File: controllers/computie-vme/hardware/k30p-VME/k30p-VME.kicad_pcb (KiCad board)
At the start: 2 copper layers, 160 x 100 mm, 87 parts, among them J1 5V, J2 5V, J3 JTAG, J4 Serial1, J5 Serial2, P1 USB_C_Plug_USB2.0, P2 USB_C_Plug_USB2.0, P3 VME64-P1-3R, SW1 ~{RESET}, SW2 SW_DIP_x06, SW3 E-Switch TL2243, U1 MC68030RC, U10 FT231XS, U11 74ABT16245DL, U12 74ABT16245DL, U13 74ABT16245DL, U14 74ABT16245DL, U15 74ABT16245DL, U16 74HC148, U2 74HC14, U3 74HC05, U4 ATF1508AS-xxAx100, U5 AS6C8016, U6 AS6C8016, U7 AM29F040, U8 MC68681, U9 FT231XS, Y1 Crystal, Y2 Crystal

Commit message: Updating with more work in progress
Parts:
- removed the D2 at (115.2, 124.0)
- removed the SW2 at (96.3, 46.1)
- added C12: 0.1uF, Capacitor_SMD:C_0805_2012Metric_Pad1.18x1.45mm_HandSolder, F.Cu at (69.8, 48.1)
- added C13: 0.1uF, Capacitor_SMD:C_0805_2012Metric_Pad1.18x1.45mm_HandSolder, F.Cu at (103.6, 36.6)
- added C14: 0.1uF, Capacitor_SMD:C_0805_2012Metric_Pad1.18x1.45mm_HandSolder, F.Cu at (88.0, 64.9)
- added C15: 0.1uF, Capacitor_SMD:C_0805_2012Metric_Pad1.18x1.45mm_HandSolder, F.Cu at (86.9, 88.8)
- added C16: 0.1uF, Capacitor_SMD:C_0805_2012Metric_Pad1.18x1.45mm_HandSolder, F.Cu at (122.2, 46.6)
- added C17: 0.1uF, Capacitor_SMD:C_0805_2012Metric_Pad1.18x1.45mm_HandSolder, F.Cu at (128.8, 46.4)
- added C18: 0.1uF, Capacitor_SMD:C_0805_2012Metric_Pad1.18x1.45mm_HandSolder, F.Cu at (159.2, 63.8)
- added C19: 0.1uF, Capacitor_SMD:C_0805_2012Metric_Pad1.18x1.45mm_HandSolder, F.Cu at (128.0, 89.4)
- added C20: 0.1uF, Capacitor_SMD:C_0805_2012Metric_Pad1.18x1.45mm_HandSolder, F.Cu at (145.5, 89.3)
- added C21: 0.1uF, Capacitor_SMD:C_0805_2012Metric_Pad1.18x1.45mm_HandSolder, F.Cu at (151.1, 101.0)
- added C22: 0.1uF, Capacitor_SMD:C_0805_2012Metric_Pad1.18x1.45mm_HandSolder, F.Cu at (123.7, 106.9)
- added C23: 0.1uF, Capacitor_SMD:C_0805_2012Metric_Pad1.18x1.45mm_HandSolder, F.Cu at (159.1, 114.7)
- added C24: 0.1uF, Capacitor_SMD:C_0805_2012Metric_Pad1.18x1.45mm_HandSolder, F.Cu at (114.2, 114.8)
- added C25: 0.1uF, Capacitor_SMD:C_0805_2012Metric_Pad1.18x1.45mm_HandSolder, F.Cu at (162.9, 37.5)
- added C26: 0.1uF, Capacitor_SMD:C_0805_2012Metric_Pad1.18x1.45mm_HandSolder, F.Cu at (162.9, 53.2)
- added C27: 0.1uF, Capacitor_SMD:C_0805_2012Metric_Pad1.18x1.45mm_HandSolder, F.Cu at (162.9, 69.3)
- added C28: 0.1uF, Capacitor_SMD:C_0805_2012Metric_Pad1.18x1.45mm_HandSolder, F.Cu at (162.9, 85.2)
- added C29: 0.1uF, Capacitor_SMD:C_0805_2012Metric_Pad1.18x1.45mm_HandSolder, F.Cu at (162.9, 101.1)
- added C30: 0.1uF, Capacitor_SMD:C_0805_2012Metric_Pad1.18x1.45mm_HandSolder, B.Cu at (141.9, 63.5)
- added C31: 0.1uF, Capacitor_SMD:C_0805_2012Metric_Pad1.18x1.45mm_HandSolder, B.Cu at (134.2, 63.5)
- added C32: 0.1uF, Capacitor_SMD:C_0805_2012Metric_Pad1.18x1.45mm_HandSolder, B.Cu at (141.9, 71.2)
- added C33: 0.1uF, Capacitor_SMD:C_0805_2012Metric_Pad1.18x1.45mm_HandSolder, B.Cu at (134.2, 71.2)
- added JP5: BG0IN, Connector_PinHeader_2.54mm:PinHeader_1x02_P2.54mm_Vertical, F.Cu at (110.9, 94.5)
- added JP6: BG0OUT, Connector_PinHeader_2.54mm:PinHeader_1x02_P2.54mm_Vertical, F.Cu at (114.6, 94.5)
- added JP7: BR0, Connector_PinHeader_2.54mm:PinHeader_1x02_P2.54mm_Vertical, F.Cu at (118.2, 94.5)
- C1: footprint Capacitor_THT:C_Disc_D3.0mm_W2.0mm_P2.50mm -> Capacitor_SMD:C_0805_2012Metric_Pad1.18x1.45mm_HandSolder
- D1: value STATUS -> Harvatek HV-32H307B; footprint LED_THT:LED_D3.0mm -> Computie_Miscellaneous:Harvatek_HV-32312-260-2SUB
- D5: renamed from D8; value OUT -> IN
- D7: renamed from D4; value IN -> OUT
- JP1: value Vcc -> CDIS; footprint Jumper:SolderJumper-2_P1.3mm_Open_RoundedPad1.0x1.5mm -> Connector_PinHeader_2.54mm:PinHeader_1x02_P2.54mm_Vertical
- JP2: value IRQ -> MMUDIS
- JP3: value ~{IACK} -> Vcc; footprint Connector_PinHeader_2.54mm:PinHeader_1x02_P2.54mm_Vertical -> Jumper:SolderJumper-2_P1.3mm_Open_RoundedPad1.0x1.5mm
- L1: value 600Ω @ 100MHz (MI0805K601R-10) -> MI0805K601R-10
- R1, R12, R13, R14, R15: value 220 -> 1k
- R16, R17, R18, R19, R2: value 1k -> 220
- SW1: footprint Button_Switch_THT:SW_PUSH_6mm -> Computie_Miscellaneous:E-Switch_TL1105
- moved TP4 127.9 mm to (113.3, 36.6)
- moved R8 125.3 mm to (142.9, 126.2), turned to 90 degrees
- moved TP3 124.8 mm to (116.5, 36.6)
- moved TP2 123.9 mm to (119.6, 36.6)
- moved R7 119.4 mm to (137.8, 126.2), turned to 90 degrees
- moved R9 119.4 mm to (135.3, 126.2), turned to 90 degrees
- moved JP3 115.9 mm to (128.8, 126.2), turned to -90 degrees
- moved R3 114.7 mm to (52.1, 44.5)
- moved JP2 114.2 mm to (128.7, 36.8)
- moved R6 113.6 mm to (132.7, 126.2), turned to 90 degrees
- moved D1 112.4 mm to (40.1, 44.5)
- moved R2 109.2 mm to (52.1, 46.9)
- moved R4 108.5 mm to (52.1, 53.8)
- moved JP4 108.2 mm to (73.0, 83.3)
- moved R10 104.2 mm to (52.1, 75.6)
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- renumbered D5 to D2, D6 to D3, D3 to D4, D7 to D6, P3 to P1, SW3 to SW2, P1 to USB1, P2 to USB2
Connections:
- D1 pad 1: GND -> ~{HALT}
- D1 pad 2: Net-(D1-A) -> Net-(D1-K1)
- D2 pad 1: Net-(D5-A1) -> Net-(D2-A1)
- D2 pad 3: Net-(D5-A2) -> Net-(D2-A2)
- D3 pad 1: Net-(D6-A1) -> Net-(D3-A1)
- D3 pad 3: Net-(D6-A2) -> Net-(D3-A2)
- D4 pad 2: Net-(D3-A) -> Net-(D4-A)
- D5 pad 1: Net-(D8-K) -> Net-(D5-K)
- D5 pad 2: Net-(D8-A) -> Net-(D5-A)
- D6 pad 2: Net-(D7-A) -> Net-(D6-A)
- D7 pad 1: Net-(D4-K) (its old number) -> Net-(D7-K)
- D7 pad 2: Net-(D4-A) -> Net-(D7-A)
- JP1 pad 1: Net-(J3-Pin_4) -> ~{CDIS}
- JP1 pad 2: +5V -> GND
- JP2 pad 1: ~{IPL1} -> ~{MMUDIS}
- JP2 pad 2: ~{SIRQ} -> GND
- JP3 pad 1: ~{IACK} -> Net-(J3-Pin_4)
- JP3 pad 2: ~{SIACK} -> +5V
- P1 pad a20: unconnected-(P3A-~{IACK}-Pada20) -> Net-(P1A-~{IACK})
- P1 pad a21: unconnected-(P3A-~{IACKIN}-Pada21) -> Net-(P1A-~{IACKIN})
- P1 pad a22: unconnected-(P3A-~{IACKOUT}-Pada22) -> Net-(P1A-~{IACKIN})
- P1 pad b12: unconnected-(P3B-~{BR0}-Padb12) -> ~{VBR0}
- P1 pad b4: unconnected-(P3B-~{BG0IN}-Padb4) -> ~{VBG0IN}
- P1 pad b5: unconnected-(P3B-~{BG0OUT}-Padb5) -> ~{VBG0OUT}
- R1 pad 1: STATUSLED -> ~{HALT}
- R1 pad 2: Net-(D1-A) -> +5V
- R12 pad 1: Net-(U9-3V3OUT) -> Net-(D2-A2)
- R12 pad 2: Net-(D3-A) -> +5V
- R13 pad 1: Net-(U10-3V3OUT) -> Net-(D2-A1)
- R13 pad 2: Net-(D4-A) -> +5V
- R14 pad 1: Net-(U9-3V3OUT) -> Net-(D3-A2)
- R14 pad 2: Net-(D7-A) -> +5V
- R15 pad 1: Net-(U10-3V3OUT) -> Net-(D3-A1)
- R15 pad 2: Net-(D8-A) -> +5V
- R16 pad 1: Net-(D5-A2) -> Net-(U9-3V3OUT)
- R16 pad 2: +5V -> Net-(D4-A)
- R17 pad 1: Net-(D5-A1) -> Net-(U10-3V3OUT)
- R17 pad 2: +5V -> Net-(D5-A)
- R18 pad 1: Net-(D6-A2) -> Net-(U9-3V3OUT)
- R18 pad 2: +5V -> Net-(D6-A)
- R19 pad 1: Net-(D6-A1) -> Net-(U10-3V3OUT)
- R19 pad 2: +5V -> Net-(D7-A)
- R2 pad 1: ~{HALT} -> GND
- R2 pad 2: +5V -> Net-(D1-K2)
- R3 pad 2: Net-(D2-K) -> Net-(D1-K1)
- RN1 pad 3: ~{BR} -> ~{AVEC}
- RN1 pad 4: ~{DSACK-EXT} -> ~{BERR}
- RN1 pad 5: ~{RESET} -> ~{DSACK0}
- RN1 pad 6: ~{AVEC} -> ~{DSACK1}
- RN1 pad 7: ~{BERR} -> Net-(RN1-R6)
- RN1 pad 8: ~{MMUDIS} -> Net-(RN1-R7)
- RN1 pad 9: ~{CDIS} -> Net-(RN1-R8)
- RN2 pad 2: ~{IPL0} -> ~{BR}
- RN2 pad 3: ~{IPL1} -> ~{DSACK-EXT}
- RN2 pad 4: ~{IPL2} -> ~{RESET}
- RN2 pad 5: ~{DSACK0} -> ~{IPL0}
- RN2 pad 6: ~{DSACK1} -> ~{IPL1}
- RN2 pad 7: Net-(RN2-R6) -> ~{IPL2}
- RN2 pad 8: Net-(RN2-R7) -> ~{MMUDIS}
- RN2 pad 9: Net-(RN2-R8) -> ~{CDIS}
- U1 pad G1: Net-(RN2-R6) -> Net-(RN1-R6)
- U1 pad J1: Net-(RN2-R7) -> Net-(RN1-R7)
- U1 pad L1: Net-(RN2-R8) -> Net-(RN1-R8)
- U10 pad 10: Net-(D4-K) (its old number) -> Net-(D5-K)
- U10 pad 17: Net-(D8-K) -> Net-(D7-K)
- U11 pad 1: AL_DIR -> GND
- U11 pad 24: AL_DIR -> GND
- U16 pad 10: unconnected-(U16-IO-Pad10) -> GND
- U16 pad 14: unconnected-(U16-GS-Pad14) -> GND
- U16 pad 15: unconnected-(U16-EO-Pad15) -> +5V
- U16 pad 16: unconnected-(U16-VCC-Pad16) -> +5V
- U16 pad 5: unconnected-(U16-EI-Pad5) -> GND
- U16 pad 6: unconnected-(U16-S2-Pad6) -> ~{VIPL2}
- U16 pad 7: unconnected-(U16-S1-Pad7) -> ~{VIPL1}
- U16 pad 8: unconnected-(U16-GND-Pad8) -> GND
- U16 pad 9: unconnected-(U16-S0-Pad9) -> ~{VIPL0}
- U3 pad 5: unconnected-(U3-Pad5) -> ~{VIACK}
- U3 pad 6: unconnected-(U3-Pad6) -> Net-(P1A-~{IACK})
- U4 pad 1: unconnected-(U4-I/O/PD1-Pad1) -> ~{VAS}
- U4 pad 10: unconnected-(U4-I/O-Pad10) -> ~{VBGOUT}
- U4 pad 100: unconnected-(U4-I/O-Pad100) -> ~{AL_OE}
- U4 pad 12: unconnected-(U4-I/O-Pad12) -> ~{VBR}
- U4 pad 13: unconnected-(U4-I/O-Pad13) -> ~{VBBSY}
- U4 pad 14: unconnected-(U4-I/O-Pad14) -> ~{VBCLR}
- U4 pad 16: unconnected-(U4-I/O-Pad16) -> VAM0
- U4 pad 17: unconnected-(U4-I/O-Pad17) -> VAM1
- U4 pad 19: unconnected-(U4-I/O-Pad19) -> VAM2
- U4 pad 2: unconnected-(U4-I/O-Pad2) -> ~{VLWORD}
- U4 pad 20: unconnected-(U4-I/O-Pad20) -> VAM3
- U4 pad 21: unconnected-(U4-I/O-Pad21) -> VAM4
- U4 pad 22: unconnected-(U4-I/O-Pad22) -> VAM5
- U4 pad 5: unconnected-(U4-I/O-Pad5) -> ~{VDS1}
- U4 pad 52: unconnected-(U4-I/O-Pad52) -> STATUSLED
- U4 pad 6: unconnected-(U4-I/O-Pad6) -> ~{VDS0}
- U4 pad 7: unconnected-(U4-I/O-Pad7) -> ~{VWRITE}
- U4 pad 8: unconnected-(U4-I/O-Pad8) -> ~{VDTACK}
- U4 pad 9: unconnected-(U4-I/O-Pad9) -> ~{VBGIN}
- U4 pad 92: unconnected-(U4-I/O-Pad92) -> MD32X_DIR
- U4 pad 93: unconnected-(U4-I/O-Pad93) -> ~{MD32X_OE}
- U4 pad 94: unconnected-(U4-I/O-Pad94) -> D16X_DIR
- U4 pad 96: unconnected-(U4-I/O-Pad96) -> ~{D16X_OE}
- U4 pad 97: unconnected-(U4-I/O-Pad97) -> DL_DIR
- U4 pad 98: unconnected-(U4-I/O-Pad98) -> ~{DL_OE}
- U4 pad 99: unconnected-(U4-I/O-Pad99) -> ~{A40X_OE}
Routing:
- removed copper zone on B.Cu, net GND
- removed copper zone on F.Cu, net GND
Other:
- copper layers 2 -> 4

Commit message: Reorganized a bit
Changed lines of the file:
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@@
 		(property "Value" "JTAG"
 			(at 1.27 12.49 90)
-			(layer "F.Fab")
+			(layer "F.SilkS")
 			(effects
 				(font
@@
 		(tags "capacitor handsolder")
 		(property "Reference" "C31"
-			(at 0 -1.651 360)
+			(at 0 -1.651 0)
 			(layer "B.SilkS")
 			(effects
@@
 		)
 		(property "Value" "0.1uF"
-			(at 0 -1.68 360)
+			(at 0 -1.68 0)
 			(layer "B.Fab")
 			(effects
@@
 		)
 		(fp_text user "${REFERENCE}"
-			(at 0 0 360)
+			(at 0 0 0)
 			(layer "B.Fab")
 			(effects
@@
 		(tags "capacitor handsolder")
 		(property "Reference" "C33"
-			(at 0 -1.651 360)
+			(at 0 -1.651 0)
 			(layer "B.SilkS")
 			(effects
@@
 		)
 		(property "Value" "0.1uF"
-			(at 0 -1.68 360)
+			(at 0 -1.68 0)
 			(layer "B.Fab")
 			(effects
@@
 		)
 		(fp_text user "${REFERENCE}"
-			(at 0 0 360)
+			(at 0 0 0)
 			(layer "B.Fab")
 			(effects

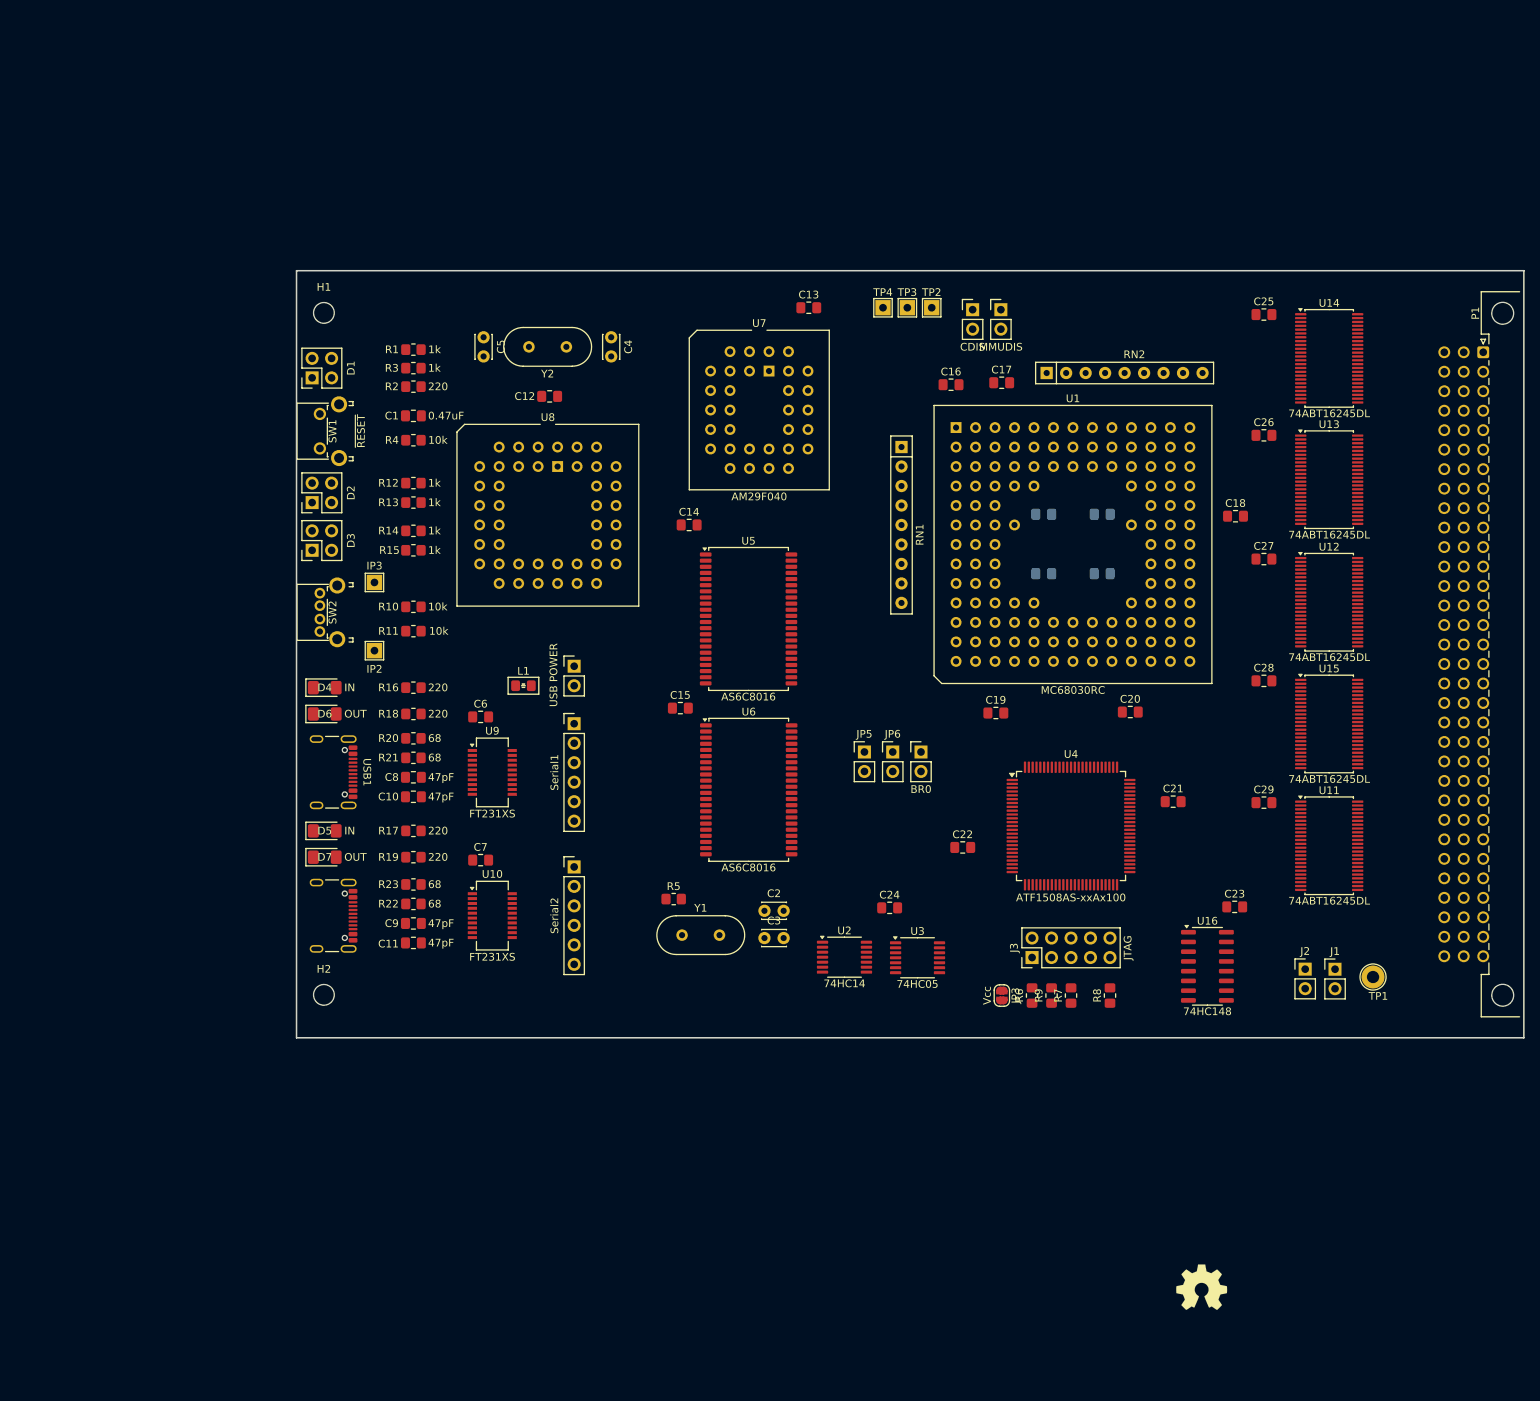
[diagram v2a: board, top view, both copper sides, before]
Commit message: Schematics for k30p-VME more or less done
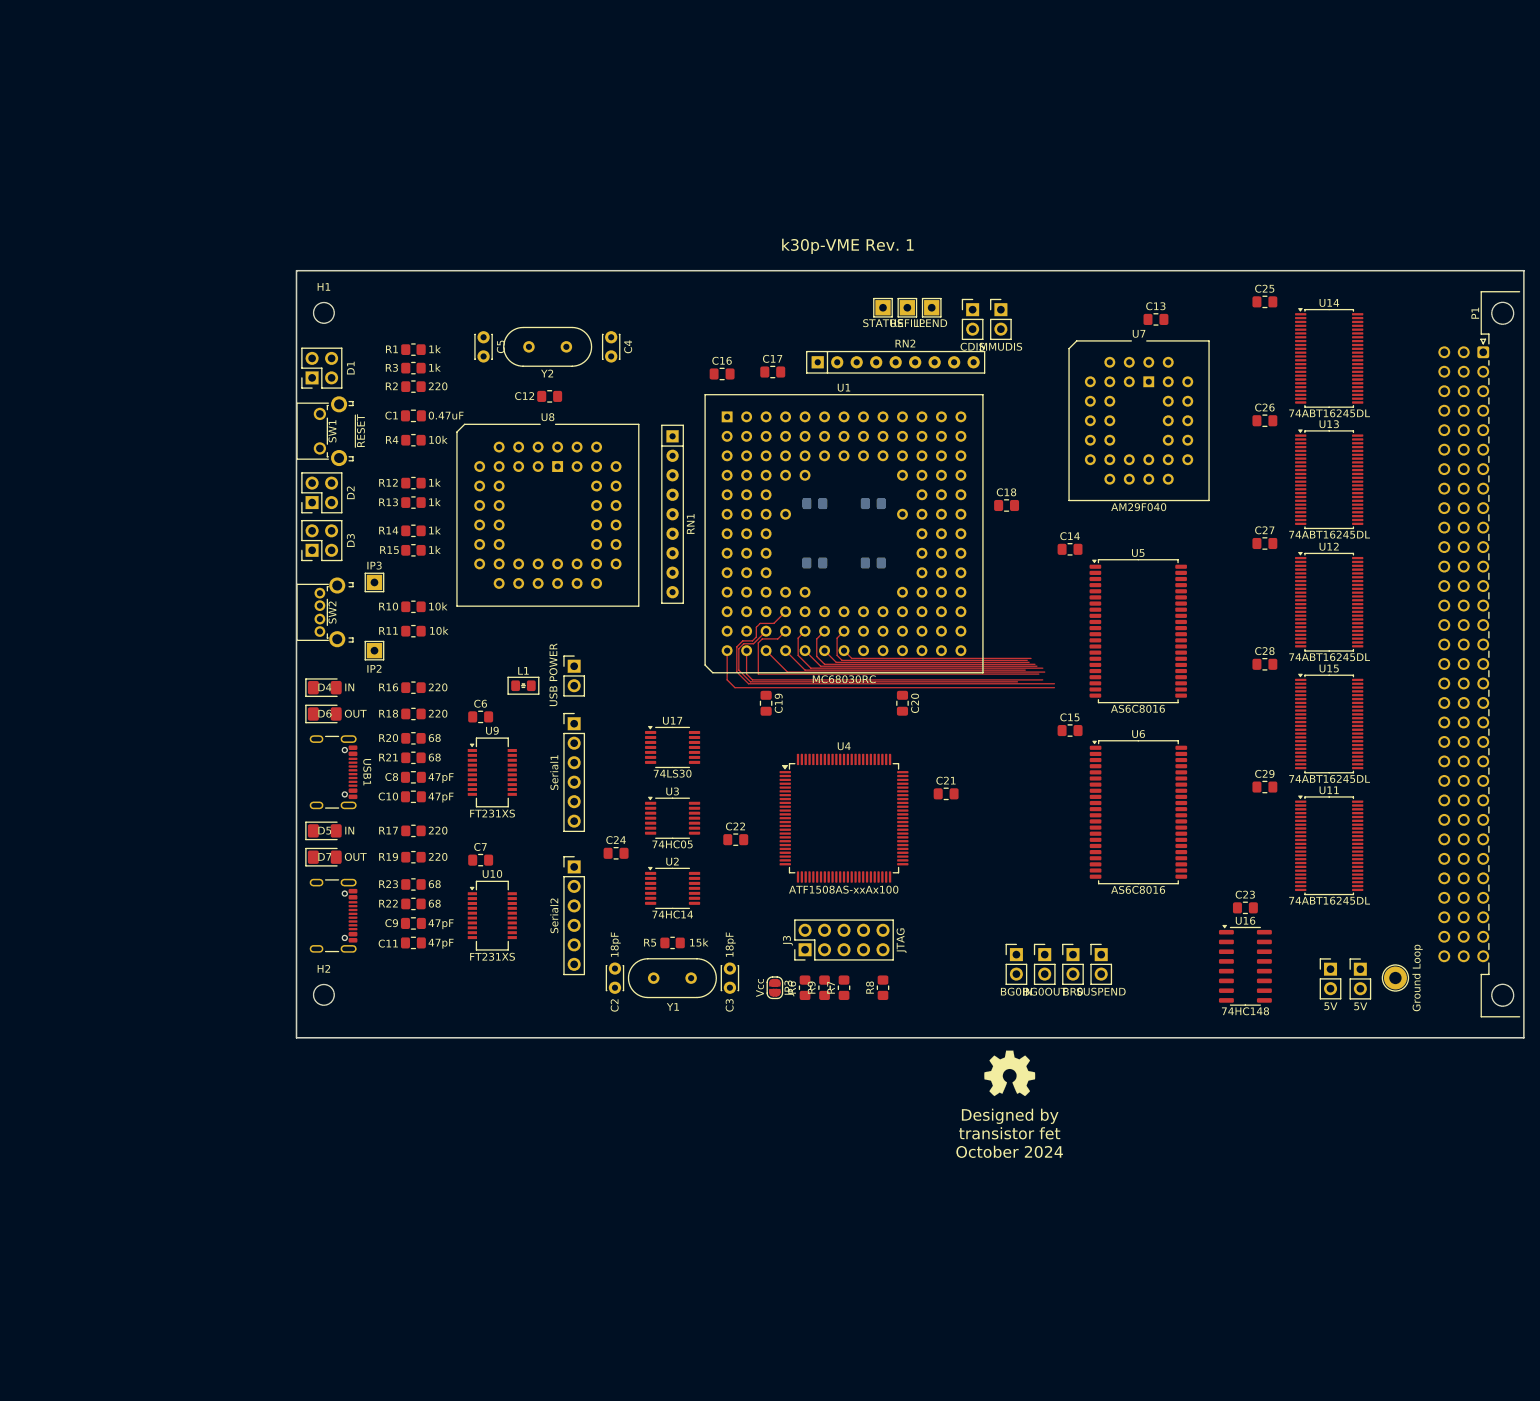
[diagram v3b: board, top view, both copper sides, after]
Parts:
- added JP8: SUSPEND, Connector_PinHeader_2.54mm:PinHeader_1x02_P2.54mm_Vertical, F.Cu at (141.7, 120.9)
- added U17: 74LS30, Package_SO:TSSOP-14_4.4x5mm_P0.65mm, F.Cu at (85.9, 93.9)
- moved U6 50.9 mm to (146.6, 102.3)
- moved C15 50.9 mm to (137.7, 91.7)
- moved U5 50.8 mm to (146.6, 78.7)
- moved C14 49.8 mm to (137.7, 68.1)
- moved U7 49.5 mm to (147.9, 46.2)
- moved C13 45.3 mm to (148.9, 38.1)
- moved S1 37.5 mm to (129.8, 136.4)
- moved U3 36.8 mm to (85.9, 103.1)
- moved C24 36.4 mm to (78.5, 107.7)
- moved JP5 33.0 mm to (130.7, 120.9)
- moved JP6 33.0 mm to (134.4, 120.9)
- moved JP7 33.0 mm to (138.0, 120.9)
- moved C19 30.0 mm to (98.0, 88.1), turned to -90 degrees
- moved C30 29.9 mm to (112.0, 62.1)
- moved C32 29.9 mm to (112.0, 69.8)
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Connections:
- J5 pad 1: UART2_DTR -> GND
- J5 pad 2: UART2_RX -> UART2_CTS
- J5 pad 3: UART2_TX -> unconnected-(J5-Pin_3-Pad3)
- J5 pad 4: unconnected-(J5-Pin_4-Pad4) -> UART2_TX
- J5 pad 5: UART2_CTS -> UART2_RX
- J5 pad 6: GND -> UART2_DTR
- JP5 pad 2: ~{VB0GIN} -> ~{VBG0IN}
- P1 pad b3: ~{VACFAIL} -> unconnected-(P1B-~{ACFAIL}-Padb3)
- P1 pad c10: ~{VSYSFAIL} -> unconnected-(P1C-~{SYSFAIL}-Padc10)
- RN2 pad 3: ~{DSACK-EXT} -> ~{RESET}
- RN2 pad 4: ~{RESET} -> ~{IPL0}
- RN2 pad 5: ~{IPL0} -> ~{IPL1}
- RN2 pad 6: ~{IPL1} -> ~{IPL2}
- RN2 pad 7: ~{IPL2} -> ~{MMUDIS}
- RN2 pad 8: ~{MMUDIS} -> ~{CDIS}
- RN2 pad 9: ~{CDIS} -> unconnected-(RN2-R8-Pad9)
- U1 pad E1: CLK -> CPU_CLK
- U1 pad M1: ~{DBEN} -> unconnected-(U1-DBEN-PadM1)
- U1 pad M2: unconnected-(U1-ECS-PadM2) -> ~{ECS}
- U16 pad 14: GND -> unconnected-(U16-GS-Pad14)
- U16 pad 15: +5V -> unconnected-(U16-EO-Pad15)
- U2 pad 10: (no net) -> unconnected-(U2-Pad10)
- U2 pad 11: (no net) -> unconnected-(U2-Pad11)
- U2 pad 14: (no net) -> +5V
- U2 pad 6: CLK -> MAIN_CLK
- U2 pad 7: (no net) -> GND
- U2 pad 8: (no net) -> Net-(U2-Pad8)
- U2 pad 9: (no net) -> ~{VSYSRESET}
- U3 pad 10: (no net) -> unconnected-(U3-Pad10)
- U3 pad 11: (no net) -> unconnected-(U3-Pad11)
- U3 pad 12: (no net) -> Net-(P1A-~{IACK})
- U3 pad 13: (no net) -> ~{VIACK}
- U3 pad 14: (no net) -> +5V
- U3 pad 5: ~{VIACK} -> unconnected-(U3-Pad5)
- U3 pad 6: Net-(P1A-~{IACK}) -> unconnected-(U3-Pad6)
- U3 pad 7: (no net) -> GND
- U3 pad 8: (no net) -> ~{RESET}
- U3 pad 9: (no net) -> Net-(U2-Pad8)
- U4 pad 1: ~{VAS} -> ~{AS}
- U4 pad 10: ~{VBGOUT} -> ~{BERR}
- U4 pad 12: ~{VBR} -> FC0
- U4 pad 13: ~{VBBSY} -> FC1
- U4 pad 14: ~{VBCLR} -> FC2
- U4 pad 16: VAM0 -> ~{BGACK}
- U4 pad 17: VAM1 -> ~{BG}
- U4 pad 19: VAM2 -> ~{BR}
- U4 pad 2: ~{VLWORD} -> ~{DS}
- U4 pad 20: VAM3 -> ~{IPL0}
- U4 pad 21: VAM4 -> ~{IPL1}
- U4 pad 22: VAM5 -> ~{IPL2}
- U4 pad 23: unconnected-(U4-I/O-Pad23) -> ~{AVEC}
- U4 pad 24: unconnected-(U4-I/O-Pad24) -> ~{RAMSEL}
- U4 pad 25: unconnected-(U4-I/O-Pad25) -> ~{ROMSEL}
- U4 pad 27: unconnected-(U4-I/O-Pad27) -> ~{IOSEL}
- U4 pad 28: unconnected-(U4-I/O-Pad28) -> ~{DS0}
- U4 pad 29: unconnected-(U4-I/O-Pad29) -> ~{DS1}
- U4 pad 30: unconnected-(U4-I/O-Pad30) -> ~{DS2}
- U4 pad 31: unconnected-(U4-I/O-Pad31) -> ~{DS3}
- U4 pad 32: unconnected-(U4-I/O-Pad32) -> ~{SIRQ}
- U4 pad 33: unconnected-(U4-I/O-Pad33) -> ~{SIACK}
- U4 pad 35: unconnected-(U4-I/O-Pad35) -> LA0
- U4 pad 36: unconnected-(U4-I/O-Pad36) -> LA1
- U4 pad 37: unconnected-(U4-I/O-Pad37) -> LA2
- U4 pad 40: unconnected-(U4-I/O-Pad40) -> LA3
- U4 pad 41: unconnected-(U4-I/O/PD2-Pad41) -> LA16
- U4 pad 42: unconnected-(U4-I/O-Pad42) -> LA17
- U4 pad 44: unconnected-(U4-I/O-Pad44) -> LA18
- U4 pad 45: unconnected-(U4-I/O-Pad45) -> LA19
- U4 pad 46: unconnected-(U4-I/O-Pad46) -> LA20
- U4 pad 47: unconnected-(U4-I/O-Pad47) -> LA21
- U4 pad 48: unconnected-(U4-I/O-Pad48) -> LA22
- U4 pad 49: unconnected-(U4-I/O-Pad49) -> LA23
- U4 pad 5: ~{VDS1} -> SIZ0
- U4 pad 50: unconnected-(U4-I/O-Pad50) -> Net-(U17-Pad8)
- U4 pad 53: unconnected-(U4-I/O-Pad53) -> IP5
- U4 pad 54: unconnected-(U4-I/O-Pad54) -> IP4
- U4 pad 55: unconnected-(U4-I/O-Pad55) -> OP3
- U4 pad 56: unconnected-(U4-I/O-Pad56) -> OP2
- U4 pad 57: unconnected-(U4-I/O-Pad57) -> ~{VIACK}
- U4 pad 58: unconnected-(U4-I/O-Pad58) -> ~{VIPL2}
- U4 pad 6: ~{VDS0} -> SIZ1
- U4 pad 60: unconnected-(U4-I/O-Pad60) -> ~{VIPL1}
- U4 pad 61: unconnected-(U4-I/O-Pad61) -> ~{VIPL0}
- U4 pad 63: unconnected-(U4-I/O-Pad63) -> ~{VBGOUT}
- U4 pad 64: unconnected-(U4-I/O-Pad64) -> ~{VBGIN}
- U4 pad 65: unconnected-(U4-I/O-Pad65) -> ~{VBR}
- U4 pad 67: unconnected-(U4-I/O-Pad67) -> VAM5
- U4 pad 68: unconnected-(U4-I/O-Pad68) -> VAM4
- U4 pad 69: unconnected-(U4-I/O-Pad69) -> VAM3
- U4 pad 7: ~{VWRITE} -> ~{WR}
- U4 pad 70: unconnected-(U4-I/O-Pad70) -> VAM2
- U4 pad 71: unconnected-(U4-I/O-Pad71) -> VAM1
- U4 pad 72: unconnected-(U4-I/O-Pad72) -> VAM0
- U4 pad 75: unconnected-(U4-I/O-Pad75) -> ~{VBERR}
- U4 pad 76: unconnected-(U4-I/O-Pad76) -> ~{VDTACK}
- U4 pad 77: unconnected-(U4-I/O-Pad77) -> ~{VWRITE}
- U4 pad 78: unconnected-(U4-I/O-Pad78) -> ~{VDS0}
- U4 pad 79: unconnected-(U4-I/O-Pad79) -> ~{VDS1}
- U4 pad 8: ~{VDTACK} -> ~{DSACK0}
- U4 pad 80: unconnected-(U4-I/O-Pad80) -> ~{VLWORD}
- U4 pad 81: unconnected-(U4-I/O-Pad81) -> ~{VAS}
- U4 pad 83: unconnected-(U4-I/O-Pad83) -> CPU_CLK
- U4 pad 84: unconnected-(U4-I/O-Pad84) -> ~{ECS}
- U4 pad 85: unconnected-(U4-I/O/GCLK3-Pad85) -> ~{VBBSY}
- U4 pad 87: CLK -> MAIN_CLK
- U4 pad 88: unconnected-(U4-I/OE1-Pad88) -> ~{RMC}
- U4 pad 89: unconnected-(U4-I/GCLR-Pad89) -> ~{RESET}
- U4 pad 9: ~{VBGIN} -> ~{DSACK1}
- U5 pad 1: A6 -> LA6
- U5 pad 10: D19 -> LD19
- U5 pad 13: D20 -> LD20
- U5 pad 14: D21 -> LD21
- U5 pad 15: D22 -> LD22
- U5 pad 16: D23 -> LD23
- U5 pad 18: A20 -> LA20
- U5 pad 19: A19 -> LA19
- U5 pad 2: A5 -> LA5
- U5 pad 20: A18 -> LA18
- U5 pad 21: A17 -> LA17
- U5 pad 22: A16 -> LA16
- U5 pad 23: A15 -> LA15
- U5 pad 24: A14 -> LA14
- U5 pad 25: A13 -> LA13
- U5 pad 26: A12 -> LA12
- U5 pad 27: A11 -> LA11
- U5 pad 28: A10 -> LA10
- U5 pad 29: D24 -> LD24
- U5 pad 3: A4 -> LA4
- U5 pad 30: D25 -> LD25
- U5 pad 31: D26 -> LD26
- U5 pad 32: D27 -> LD27
- U5 pad 35: D28 -> LD28
- U5 pad 36: D29 -> LD29
- U5 pad 37: D30 -> LD30
- U5 pad 38: D31 -> LD31
- U5 pad 4: A3 -> LA3
- U5 pad 42: A9 -> LA9
- U5 pad 43: A8 -> LA8
- U5 pad 44: A7 -> LA7
- U5 pad 5: A2 -> LA2
- U5 pad 7: D16 -> LD16
- U5 pad 8: D17 -> LD17
- U5 pad 9: D18 -> LD18
- U6 pad 1: A6 -> LA6
- U6 pad 10: D3 -> LD3
- U6 pad 13: D4 -> LD4
- U6 pad 14: D5 -> LD5
- U6 pad 15: D6 -> LD6
- U6 pad 16: D7 -> LD7
- U6 pad 18: A20 -> LA20
- U6 pad 19: A19 -> LA19
- U6 pad 2: A5 -> LA5
- U6 pad 20: A18 -> LA18
- U6 pad 21: A17 -> LA17
- U6 pad 22: A16 -> LA16
- U6 pad 23: A15 -> LA15
- U6 pad 24: A14 -> LA14
- U6 pad 25: A13 -> LA13
- U6 pad 26: A12 -> LA12
- U6 pad 27: A11 -> LA11
- U6 pad 28: A10 -> LA10
- U6 pad 29: D8 -> LD8
- U6 pad 3: A4 -> LA4
- U6 pad 30: D9 -> LD9
- U6 pad 31: D10 -> LD10
- U6 pad 32: D11 -> LD11
- U6 pad 35: D12 -> LD12
- U6 pad 36: D13 -> LD13
- U6 pad 37: D14 -> LD14
- U6 pad 38: D15 -> LD15
- U6 pad 4: A3 -> LA3
- U6 pad 42: A9 -> LA9
- U6 pad 43: A8 -> LA8
- U6 pad 44: A7 -> LA7
- U6 pad 5: A2 -> LA2
- U6 pad 7: D0 -> LD0
- U6 pad 8: D1 -> LD1
- U6 pad 9: D2 -> LD2
- U7 pad 1: A18 -> LA18
- U7 pad 10: A2 -> LA2
- U7 pad 11: A1 -> LA1
- U7 pad 12: A0 -> LA0
- U7 pad 13: D24 -> LD24
- U7 pad 14: D25 -> LD25
- U7 pad 15: D26 -> LD26
- U7 pad 17: D27 -> LD27
- U7 pad 18: D28 -> LD28
- U7 pad 19: D29 -> LD29
- U7 pad 2: A16 -> LA16
- U7 pad 20: D30 -> LD30
- U7 pad 21: D31 -> LD31
- U7 pad 23: A10 -> LA10
- U7 pad 25: A11 -> LA11
- U7 pad 26: A9 -> LA9
- U7 pad 27: A8 -> LA8
- U7 pad 28: A13 -> LA13
- U7 pad 29: A14 -> LA14
- U7 pad 3: A15 -> LA15
- U7 pad 30: A17 -> LA17
- U7 pad 4: A12 -> LA12
- U7 pad 5: A7 -> LA7
- U7 pad 6: A6 -> LA6
- U7 pad 7: A5 -> LA5
- U7 pad 8: A4 -> LA4
- U7 pad 9: A3 -> LA3
- U8 pad 18: D25 -> LD25
- U8 pad 19: D27 -> LD27
- U8 pad 2: A1 -> LA1
- U8 pad 20: D29 -> LD29
- U8 pad 21: D31 -> LD31
- U8 pad 25: D30 -> LD30
- U8 pad 26: D28 -> LD28
- U8 pad 27: D26 -> LD26
- U8 pad 28: D24 -> LD24
- U8 pad 4: A2 -> LA2
- U8 pad 6: A3 -> LA3
- U8 pad 7: A4 -> LA4
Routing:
- net LD30: track 0.00 -> 54.3 mm
- net LD31: track 0.00 -> 46.9 mm
- net LD27: track 0.00 -> 44.8 mm
- net LD29: track 0.00 -> 44.3 mm
- net LD28: track 0.00 -> 42.0 mm
- net LD26: track 0.00 -> 37.5 mm
- net LD24: track 0.00 -> 36.1 mm
- net LD22: track 0.00 -> 32.6 mm
- net LD25: track 0.00 -> 32.3 mm
- net LD23: track 0.00 -> 31.1 mm
- net LD20: track 0.00 -> 28.6 mm
- net LD21: track 0.00 -> 27.3 mm
- net LD19: track 0.00 -> 24.8 mm
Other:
- board text added: "Designed by transistor fet October 2024"
- board text added: "k30p-VME Rev. 1"
